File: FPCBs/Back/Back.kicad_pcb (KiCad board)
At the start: 2 copper layers, 131.9 x 112.1 mm, 26 parts, among them J1 To PCB, J2 To Front, J3 Front, J5 From LCD, J6 To Right, SW1 MENU/SET, SW10 -+-, SW11 PLAY, SW13 S/C/M, SW14 ON/OFF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

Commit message: Fix connectors
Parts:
- moved J5 10.2 mm to (77.3, 99.0), turned to 0 degrees
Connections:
- SW13 pad 2: Net-(J3-Pin_2) -> Net-(J3-Pin_3)
- SW13 pad 3: Net-(J3-Pin_3) -> Net-(J3-Pin_2)
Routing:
- net Net-(J1-Pin_34): track 89.2 -> 48.0 mm
- net Net-(J1-Pin_33): track 87.3 -> 49.8 mm
- net Net-(J1-Pin_32): track 87.2 -> 51.2 mm
- net Net-(J3-Pin_1): track 86.1 -> 73.2 mm
- net Net-(J3-Pin_2): track 75.2 -> 68.2 mm
- net Net-(J3-Pin_3): track 68.1 -> 74.8 mm
- net Net-(J2-Pin_4): track 41.5 -> 45.3 mm
- net Net-(J2-Pin_5): track 41.5 -> 44.6 mm
- net Net-(J5-Pin_2): track 74.0 -> 76.1 mm
- net Net-(J5-Pin_1): track 71.1 -> 72.4 mm
- net Net-(J1-Pin_30): track 177.0 -> 176.1 mm
- net Net-(J1-Pin_7): track 108.5 -> 109.3 mm
- added copper zone on F.Cu, net Net-(J1-Pin_28)

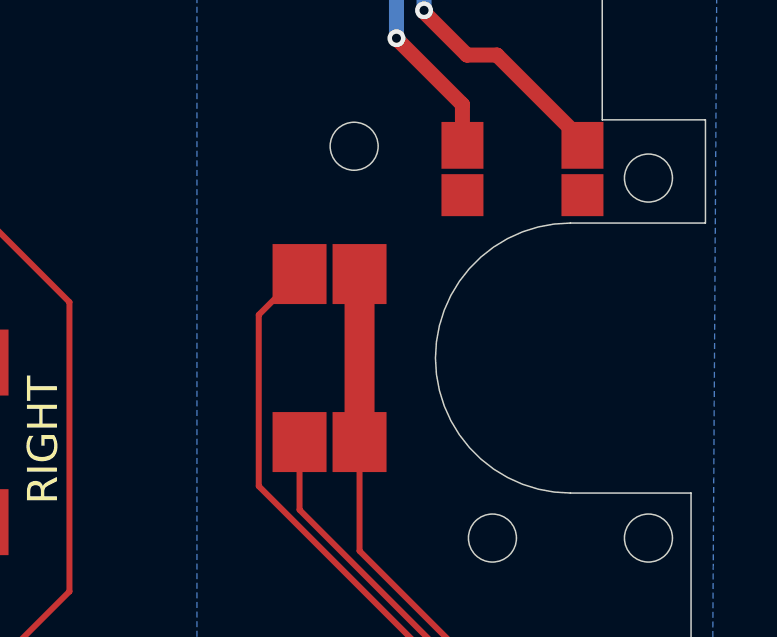
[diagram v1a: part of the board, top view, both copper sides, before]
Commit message: Add holes to switch detectors
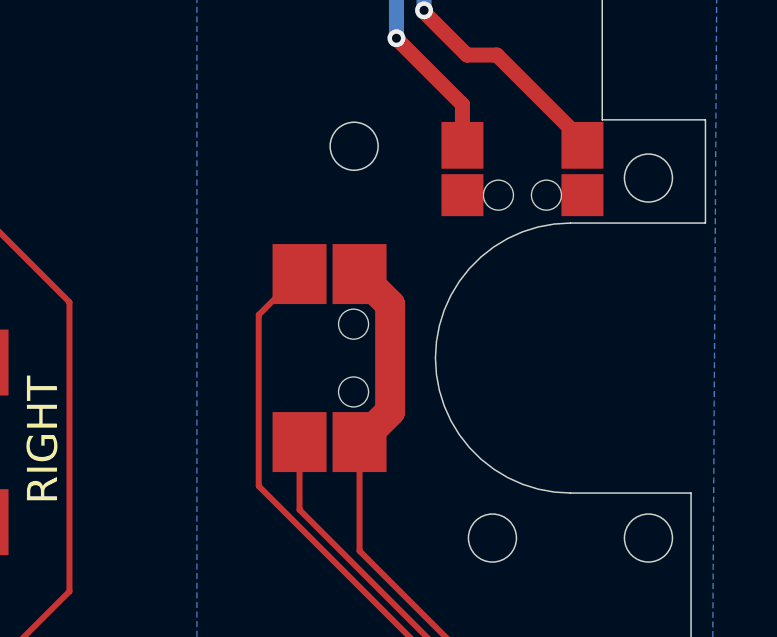
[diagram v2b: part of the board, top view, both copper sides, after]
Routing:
- net Net-(J3-Pin_1): track 73.2 -> 74.0 mm
